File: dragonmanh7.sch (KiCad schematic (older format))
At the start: 149 parts, among them J1 USB_C, J10 Conn_02x12_Odd_Even, J11 Conn_02x05_Odd_Even, J12 VBAT+, J13 Conn_02x05_Odd_Even, J14 VBATG, J15 Conn_02x02_Odd_Even, J16 Conn_02x02_Odd_Even, J18 Conn_02x05_Odd_Even, J2 73725-0110BLF, J3 RJ45_Amphenol_RJMG1BD3B8K1ANR, J4 105162-0001, J5 Screw_Terminal_01x06, J6 Conn_02x12_Odd_Even, J7 USB_C, J8 Screw_Terminal_01x02, J9 Conn_02x12_Odd_Even, SW1 RESET, SW2 PC13, U1 STM32H743VITx, U10 USBLC6-2SC6, U12 TCAN332, U13 ISL83483, U14 MIC2005A, U2 LAN8742A-CZ-TR, U3 AZ1117CD-3.3TRG1, U5 S25FL127SABMFI101, U6 AP63205, U7 USBLC6-2SC6, U8 STM32F042F6Px, U9 USBLC6-2SC6, Y1 8MHz, Y2 32.768KHz, Y3 25MHz

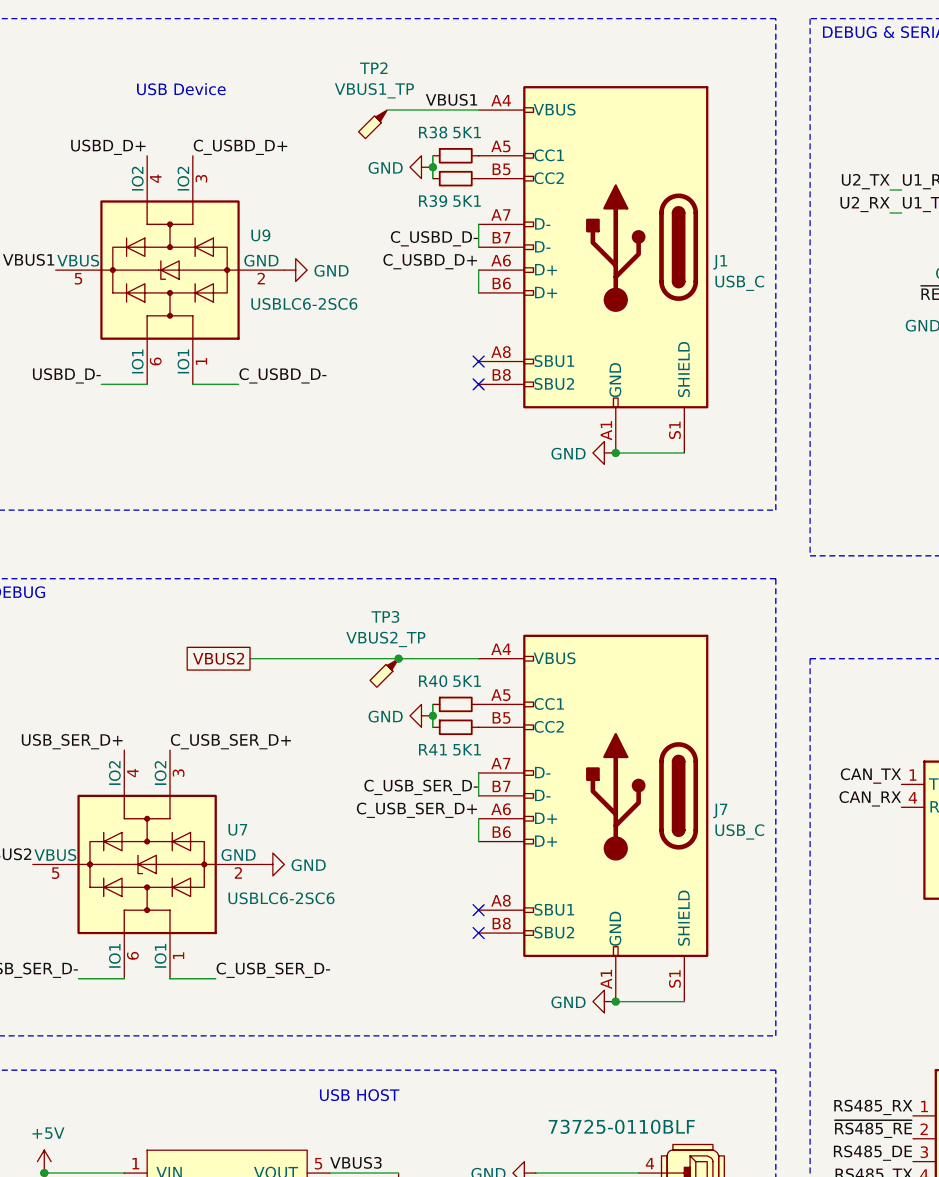
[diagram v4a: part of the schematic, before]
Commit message: Change usb-c to old usb-b connectors, move uSD to outter
Signed-off-by: Martin Ribelotta <martinribelotta@gmail.com>
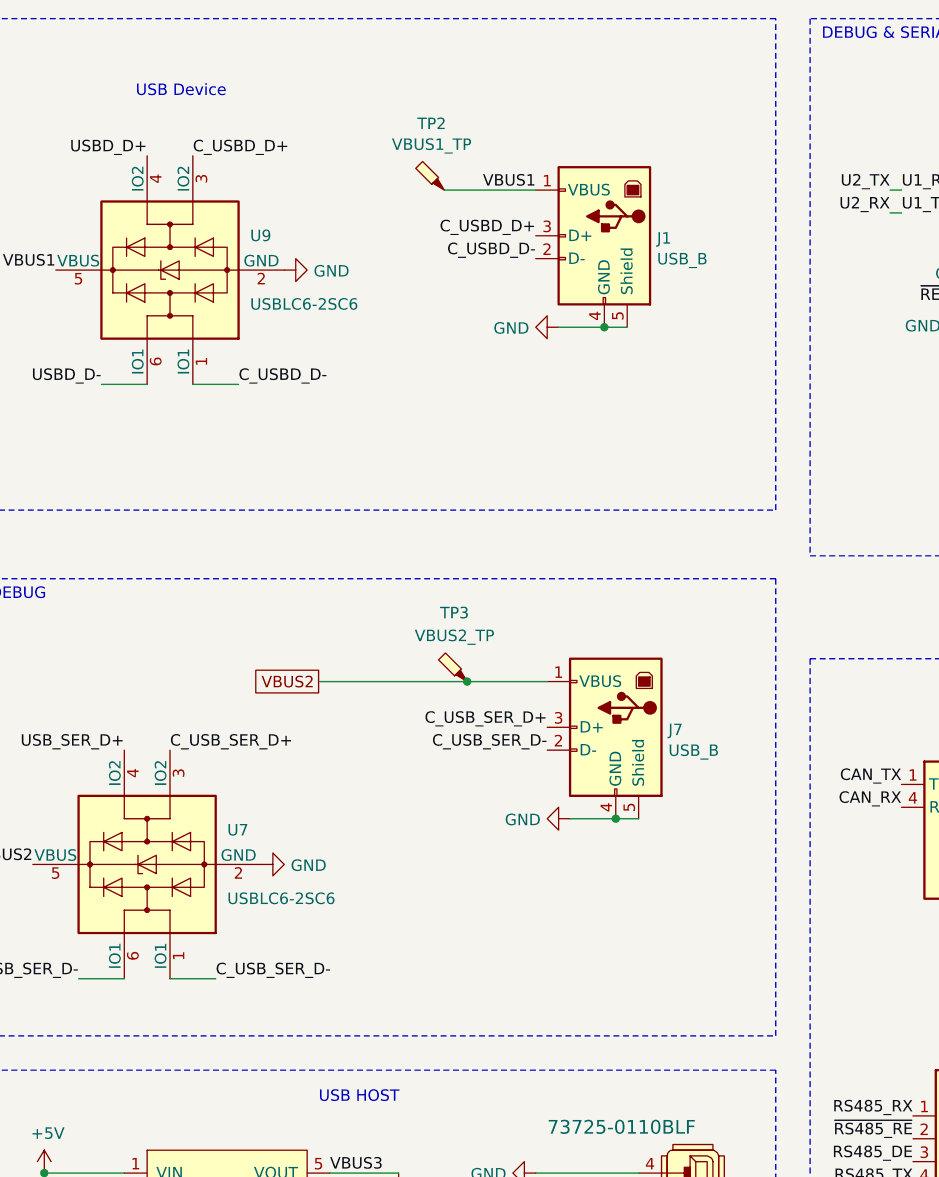
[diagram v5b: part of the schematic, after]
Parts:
- removed J1, J7: USB_C, Connector_USB:USB_C_Receptacle_Palconn_UTC16-G, symbol dragonmanh7-rescue:USB_C_Receptacle_USB2.0-Connector
- removed R38, R39, R40, R41: 5K1, Resistor_SMD:R_0603_1608Metric, symbol Device:R_Small
- added J1, J7: USB_B, Connector_USB:USB_B_Lumberg_2411_02_Horizontal, symbol Connector:USB_B
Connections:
- net C_USBD_D+: now also J1.3 (D+)
- net C_USBD_D-: now also J1.2 (D-)
- net C_USB_SER_D+: now also J7.3 (D+)
- net C_USB_SER_D-: now also J7.2 (D-)
- net GND: now also J1.4 (GND), J1.5 (Shield), J7.4 (GND), J7.5 (Shield)
- net VBUS1: now also J1.1 (VBUS)
- net VBUS2: now also J7.1 (VBUS)
- no-connect marks 10 -> 6
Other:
- moved on the sheet: TP2, TP3
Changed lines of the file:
@@
 Text Label 3750 2550 0    50   ~ 0
 U1_RX
-Text Label 10850 4050 2    50   ~ 0
+Text Label 11150 3650 2    50   ~ 0
 C_USB_SER_D+
-Text Label 10850 3950 2    50   ~ 0
+Text Label 11150 3750 2    50   ~ 0
 C_USB_SER_D-
 $Comp
@@
 L Connector:TestPoint_Probe TP3
 U 1 1 5E1FA9DD
-P 10500 3350
-F 0 "TP3" V 10319 3405 50  0000 C CNN
-F 1 "VBUS2_TP" V 10410 3405 50  0000 C CNN
-F 2 "TestPoint:TestPoint_Pad_D2.5mm" H 10700 3350 50  0001 C CNN
-F 3 "~" H 10700 3350 50  0001 C CNN
-	1    10500 3350
-	0    -1   1    0
+P 10800 3450
+F 0 "TP3" H 10855 3750 50  0000 C CNN
+F 1 "VBUS2_TP" H 10855 3650 50  0000 C CNN
+F 2 "TestPoint:TestPoint_Pad_D2.5mm" H 11000 3450 50  0001 C CNN
+F 3 "~" H 11000 3450 50  0001 C CNN
+	1    10800 3450
+	-1   0    0    -1
 $EndComp
 Wire Wire Line
-	10500 3350 10850 3350
+	10800 3450 11150 3450
 $Comp
 L Connector:TestPoint_Probe TP4
@@
 L power:GND #PWR032
 U 1 1 611E4C91
-P 11450 4850
-F 0 "#PWR032" H 11450 4600 50  0001 C CNN
-F 1 "GND" V 11455 4722 50  0000 R CNN
-F 2 "" H 11450 4850 50  0001 C CNN
-F 3 "" H 11450 4850 50  0001 C CNN
-	1    11450 4850
+P 11250 4050
+F 0 "#PWR032" H 11250 3800 50  0001 C CNN
+F 1 "GND" V 11255 3922 50  0000 R CNN
+F 2 "" H 11250 4050 50  0001 C CNN
+F 3 "" H 11250 4050 50  0001 C CNN
+	1    11250 4050
 	0    1    1    0
 $EndComp
-$Comp
-L dragonmanh7-rescue:USB_C_Receptacle_USB2.0-Connector J7
-U 1 1 611E4C9F
-P 11450 3950
-F 0 "J7" H 11020 3889 50  0000 R CNN
-F 1 "USB_C" H 11020 3798 50  0000 R CNN
-F 2 "Connector_USB:USB_C_Receptacle_Palconn_UTC16-G" H 11600 3950 50  0001 C CNN
-F 3 "https://www.usb.org/sites/default/files/documents/usb_type-c.zip" H 11600 3950 50  0001 C CNN
-	1    11450 3950
-	-1   0    0    -1
-$EndComp
-Wire Wire Line
-	10850 3850 10850 3950
-Wire Wire Line
-	10850 4050 10850 4150
-NoConn ~ 10850 4450
-NoConn ~ 10850 4550
-$Comp
-L Device:R_Small R40
-U 1 1 611E4CAA
-P 10750 3550
-F 0 "R40" V 10650 3650 50  0000 C CNN
-F 1 "5K1" V 10650 3500 50  0000 C CNN
-F 2 "Resistor_SMD:R_0603_1608Metric" H 10750 3550 50  0001 C CNN
-F 3 "~" H 10750 3550 50  0001 C CNN
-F 4 "CRGCQ0805J22R" H 2000 1350 50  0001 C CNN "manf#"
-	1    10750 3550
-	0    -1   1    0
-$EndComp
-$Comp
-L Device:R_Small R41
-U 1 1 611E4CB1
-P 10750 3650
-F 0 "R41" V 10850 3750 50  0000 C CNN
-F 1 "5K1" V 10850 3600 50  0000 C CNN
-F 2 "Resistor_SMD:R_0603_1608Metric" H 10750 3650 50  0001 C CNN
-F 3 "~" H 10750 3650 50  0001 C CNN
-F 4 "CRGCQ0805J22R" H 2000 1450 50  0001 C CNN "manf#"
-	1    10750 3650
-	0    -1   1    0
-$EndComp
 Wire Wire Line
-	10650 3650 10650 3600
-$Comp
-L power:GND #PWR031
-U 1 1 611E4CB8
-P 10650 3600
-F 0 "#PWR031" H 10650 3350 50  0001 C CNN
-F 1 "GND" V 10655 3472 50  0000 R CNN
-F 2 "" H 10650 3600 50  0001 C CNN
-F 3 "" H 10650 3600 50  0001 C CNN
-	1    10650 3600
-	0    1    1    0
-$EndComp
-Connection ~ 10650 3600
-Wire Wire Line
-	10650 3600 10650 3550
-Wire Wire Line
-	11450 4850 11750 4850
-Connection ~ 11450 4850
+	11250 4050 11450 4050
 Text Label 6850 9200 2    50   ~ 0
 PHY_RXD0
@@
 Wire Wire Line
 	6450 9200 6850 9200
-Connection ~ 11450 2450
-Wire Wire Line
-	11450 2450 11750 2450
-Wire Wire Line
-	10650 1200 10650 1150
-Connection ~ 10650 1200
-$Comp
-L power:GND #PWR030
-U 1 1 61095AE4
-P 10650 1200
-F 0 "#PWR030" H 10650 950 50  0001 C CNN
-F 1 "GND" V 10655 1072 50  0000 R CNN
-F 2 "" H 10650 1200 50  0001 C CNN
-F 3 "" H 10650 1200 50  0001 C CNN
-	1    10650 1200
-	0    1    1    0
-$EndComp
-Wire Wire Line
-	10650 1250 10650 1200
-$Comp
-L Device:R_Small R39
-U 1 1 610702FD
-P 10750 1250
-F 0 "R39" V 10850 1350 50  0000 C CNN
-F 1 "5K1" V 10850 1200 50  0000 C CNN
-F 2 "Resistor_SMD:R_0603_1608Metric" H 10750 1250 50  0001 C CNN
-F 3 "~" H 10750 1250 50  0001 C CNN
-F 4 "CRGCQ0805J22R" H 2000 -950 50  0001 C CNN "manf#"
-	1    10750 1250
-	0    -1   1    0
-$EndComp
-$Comp
-L Device:R_Small R38
-U 1 1 6105141A
-P 10750 1150
-F 0 "R38" V 10650 1250 50  0000 C CNN
-F 1 "5K1" V 10650 1100 50  0000 C CNN
-F 2 "Resistor_SMD:R_0603_1608Metric" H 10750 1150 50  0001 C CNN
-F 3 "~" H 10750 1150 50  0001 C CNN
-F 4 "CRGCQ0805J22R" H 2000 -1050 50  0001 C CNN "manf#"
-	1    10750 1150
-	0    -1   1    0
-$EndComp
-NoConn ~ 10850 2150
-NoConn ~ 10850 2050
-Wire Wire Line
-	10850 1650 10850 1750
 Wire Wire Line
-	10850 1450 10850 1550
-$Comp
-L dragonmanh7-rescue:USB_C_Receptacle_USB2.0-Connector J1
-U 1 1 60FA9730
-P 11450 1550
-F 0 "J1" H 11020 1489 50  0000 R CNN
-F 1 "USB_C" H 11020 1398 50  0000 R CNN
-F 2 "Connector_USB:USB_C_Receptacle_Palconn_UTC16-G" H 11600 1550 50  0001 C CNN
-F 3 "https://www.usb.org/sites/default/files/documents/usb_type-c.zip" H 11600 1550 50  0001 C CNN
-	1    11450 1550
-	-1   0    0    -1
-$EndComp
+	11200 1900 11400 1900
 Wire Wire Line
-	10850 950  10450 950
+	11100 1300 10700 1300
 $Comp
 L Connector:TestPoint_Probe TP2
 U 1 1 5E213482
-P 10450 950
-F 0 "TP2" V 10269 1005 50  0000 C CNN
-F 1 "VBUS1_TP" V 10360 1005 50  0000 C CNN
-F 2 "TestPoint:TestPoint_Pad_D2.5mm" H 10650 950 50  0001 C CNN
-F 3 "~" H 10650 950 50  0001 C CNN
-	1    10450 950
-	0    -1   1    0
+P 10700 1300
+F 0 "TP2" H 10755 1590 50  0000 C CNN
+F 1 "VBUS1_TP" H 10755 1499 50  0000 C CNN
+F 2 "TestPoint:TestPoint_Pad_D2.5mm" H 10900 1300 50  0001 C CNN
+F 3 "~" H 10900 1300 50  0001 C CNN
+	1    10700 1300
+	-1   0    0    -1
 $EndComp
-Text Label 10850 950  2    50   ~ 0
+Text Label 11100 1300 2    50   ~ 0
 VBUS1
 $Comp
 L power:GND #PWR0114
 U 1 1 5C5D01D3
-P 11450 2450
-F 0 "#PWR0114" H 11450 2200 50  0001 C CNN
-F 1 "GND" V 11455 2322 50  0000 R CNN
-F 2 "" H 11450 2450 50  0001 C CNN
-F 3 "" H 11450 2450 50  0001 C CNN
-	1    11450 2450
+P 11200 1900
+F 0 "#PWR0114" H 11200 1650 50  0001 C CNN
+F 1 "GND" V 11205 1772 50  0000 R CNN
+F 2 "" H 11200 1900 50  0001 C CNN
+F 3 "" H 11200 1900 50  0001 C CNN
+	1    11200 1900
 	0    1    1    0
 $EndComp
-Text Label 10850 1650 2    50   ~ 0
-C_USBD_D+
-Text Label 10850 1550 2    50   ~ 0
-C_USBD_D-
 Connection ~ 8950 5800
 Wire Notes Line
@@
 VBUS1
 Wire Wire Line
-	9850 3350 10500 3350
-Connection ~ 10500 3350
-Text GLabel 9850 3350 0    50   UnSpc ~ 0
+	10150 3450 10800 3450
+Connection ~ 10800 3450
+Text GLabel 10150 3450 0    50   UnSpc ~ 0
 VBUS2
 $Comp
@@
 	7850 1050 7850 1150
 Connection ~ 7850 1150
+$Comp
+L Connector:USB_B J7
+U 1 1 5FBCFDBB
+P 11450 3650
+F 0 "J7" H 11220 3639 50  0000 R CNN
+F 1 "USB_B" H 11220 3548 50  0000 R CNN
+F 2 "Connector_USB:USB_B_Lumberg_2411_02_Horizontal" H 11600 3600 50  0001 C CNN
+F 3 " ~" H 11600 3600 50  0001 C CNN
+	1    11450 3650
+	-1   0    0    -1
+$EndComp
+Connection ~ 11450 4050
+Wire Wire Line
+	11450 4050 11550 4050
+$Comp
+L Connector:USB_B J1
+U 1 1 5FCDADF9
+P 11400 1500
+F 0 "J1" H 11170 1489 50  0000 R CNN
+F 1 "USB_B" H 11170 1398 50  0000 R CNN
+F 2 "Connector_USB:USB_B_Lumberg_2411_02_Horizontal" H 11550 1450 50  0001 C CNN
+F 3 " ~" H 11550 1450 50  0001 C CNN
+	1    11400 1500
+	-1   0    0    -1
+$EndComp
+Connection ~ 11400 1900
+Wire Wire Line
+	11400 1900 11500 1900
+Text Label 11100 1500 2    50   ~ 0
+C_USBD_D+
+Text Label 11100 1600 2    50   ~ 0
+C_USBD_D-
 $EndSCHEMATC

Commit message: Saved point
Signed-off-by: Martin Ribelotta <martinribelotta@gmail.com>
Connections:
- net 8MHz+: now reaches C12.1, U1.12 (PH0), Y1.2
- net 8MHz-: now reaches C13.1, U1.13 (PH1), Y1.1
- net 32K-: now reaches C15.1, U1.8 (PC14), Y2.1
- net 32K+: now reaches C14.1, U1.9 (PC15), Y2.2
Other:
- moved on the sheet: C14, C15, Y2
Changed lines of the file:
@@
 L Device:Crystal_Small Y2
 U 1 1 5C5A7B9A
-P 3850 6500
-F 0 "Y2" H 3900 6600 50  0000 R CNN
-F 1 "32.768KHz" H 3700 6500 50  0000 R CNN
-F 2 "Crystal:Crystal_SMD_MicroCrystal_CC7V-T1A-2Pin_3.2x1.5mm" H 3850 6500 50  0001 C CNN
-F 3 "~" H 3850 6500 50  0001 C CNN
-F 4 "FC-135 32.7680KA-A5" H 50  0   50  0001 C CNN "manf#"
-	1    3850 6500
+P 4100 6600
+F 0 "Y2" H 4150 6700 50  0000 R CNN
+F 1 "32.768KHz" H 3950 6600 50  0000 R CNN
+F 2 "Crystal:Crystal_SMD_MicroCrystal_CC7V-T1A-2Pin_3.2x1.5mm" H 4100 6600 50  0001 C CNN
+F 3 "~" H 4100 6600 50  0001 C CNN
+F 4 "FC-135 32.7680KA-A5" H 300 100 50  0001 C CNN "manf#"
+	1    4100 6600
 	-1   0    0    -1
 $EndComp
@@
 L Device:C_Small C14
 U 1 1 5C5A7BA0
-P 3750 6650
-F 0 "C14" H 3900 6700 50  0000 C CNN
-F 1 "10p" H 3900 6600 50  0000 C CNN
-F 2 "Capacitor_SMD:C_0603_1608Metric" H 3750 6650 50  0001 C CNN
-F 3 "~" H 3750 6650 50  0001 C CNN
-F 4 "885012007010" H 50  0   50  0001 C CNN "manf#"
-	1    3750 6650
+P 4000 6750
+F 0 "C14" H 4150 6800 50  0000 C CNN
+F 1 "10p" H 4150 6700 50  0000 C CNN
+F 2 "Capacitor_SMD:C_0603_1608Metric" H 4000 6750 50  0001 C CNN
+F 3 "~" H 4000 6750 50  0001 C CNN
+F 4 "885012007010" H 300 100 50  0001 C CNN "manf#"
+	1    4000 6750
 	-1   0    0    -1
 $EndComp
@@
 L Device:C_Small C15
 U 1 1 5C5A7BA6
-P 3950 6650
-F 0 "C15" H 3800 6700 50  0000 C CNN
-F 1 "10p" H 3800 6600 50  0000 C CNN
-F 2 "Capacitor_SMD:C_0603_1608Metric" H 3950 6650 50  0001 C CNN
-F 3 "~" H 3950 6650 50  0001 C CNN
-F 4 "885012007010" H 50  0   50  0001 C CNN "manf#"
-	1    3950 6650
+P 4200 6750
+F 0 "C15" H 4050 6800 50  0000 C CNN
+F 1 "10p" H 4050 6700 50  0000 C CNN
+F 2 "Capacitor_SMD:C_0603_1608Metric" H 4200 6750 50  0001 C CNN
+F 3 "~" H 4200 6750 50  0001 C CNN
+F 4 "885012007010" H 300 100 50  0001 C CNN "manf#"
+	1    4200 6750
 	-1   0    0    -1
 $EndComp
@@
 L power:GND #PWR0112
 U 1 1 5C5A7BB6
-P 3850 6750
-F 0 "#PWR0112" H 3850 6500 50  0001 C CNN
-F 1 "GND" H 3950 6600 50  0000 R CNN
-F 2 "" H 3850 6750 50  0001 C CNN
-F 3 "" H 3850 6750 50  0001 C CNN
-	1    3850 6750
+P 4100 6850
+F 0 "#PWR0112" H 4100 6600 50  0001 C CNN
+F 1 "GND" H 4200 6700 50  0000 R CNN
+F 2 "" H 4100 6850 50  0001 C CNN
+F 3 "" H 4100 6850 50  0001 C CNN
+	1    4100 6850
 	-1   0    0    -1
 $EndComp
@@
 	1150 3000 1150 3100
 Wire Wire Line
-	3750 6350 3950 6350
+	4000 6850 4100 6850
+Connection ~ 4100 6850
 Wire Wire Line
-	3750 6750 3850 6750
-Connection ~ 3850 6750
+	4100 6850 4200 6850
 Wire Wire Line
-	3850 6750 3950 6750
-Wire Wire Line
-	3950 6500 3950 6550
-Wire Wire Line
-	3750 6550 3750 6500
-Wire Wire Line
-	3750 6450 3750 6500
-Connection ~ 3750 6500
-Wire Wire Line
-	3950 6350 3950 6500
-Connection ~ 3950 6500
+	4200 6600 4200 6650
+Connection ~ 4200 6600
 Text Label 3750 5750 0    50   ~ 0
 SDMMC_D0
@@
 Text Label 11100 1600 2    50   ~ 0
 C_USBD_D-
+Text Label 1650 2900 0    50   ~ 0
+8MHz+
+Text Label 1500 3100 3    50   ~ 0
+8MHz-
+Wire Wire Line
+	3750 6450 4000 6450
+Wire Wire Line
+	4000 6450 4000 6600
+Connection ~ 4000 6600
+Wire Wire Line
+	4000 6600 4000 6650
+Wire Wire Line
+	3750 6350 4200 6350
+Wire Wire Line
+	4200 6350 4200 6600
+Text Label 3750 6450 0    50   ~ 0
+32K+
+Text Label 3750 6350 0    50   ~ 0
+32K-
 $EndSCHEMATC
